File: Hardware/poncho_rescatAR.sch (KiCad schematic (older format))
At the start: 20 parts

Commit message: Arreglos en base a los hablado con el profesor
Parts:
- removed C? (x2): 100nF, ~, symbol C
- removed P?: CONN_4, symbol CONN_4
- removed R? (x2): 10k, ~, symbol R
- removed R? (x2): 1k, ~, symbol R
- removed SW? (x2): SW_PUSH, ~, symbol SW_PUSH
- removed U?: LM317AH, TO-39, symbol LM317AH
- added C1: 0.1u, ~, symbol CP1
- added D2, D3: DIODE, ~, symbol DIODE
- added JP1: JUMPER3, ~, symbol JUMPER3
- added P1: CONN_I2C, symbol CONN_5
- added R4: 10k, ~, symbol R
- gave numbers to parts that had none: 6
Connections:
- net labels added: 3.8V_II, UART2_RXD, UART2_TXD, VCC, VCC_3.8V_I, VCC_5V_EXT
- net labels removed: +3.3V, +5V, GNDA
- wire segments 166 -> 153
- no-connect marks 87 -> 95
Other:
- note added: "Bateria de celular:"
- note added: "Este conector es para\nagregar el modulo GPS\n"
- note added: "Estos son los\nAnalog_GND\nque no usamos"
- note added: "Fuente externa\npara la ciaa tambien"
- note added: "Habria que ver esto si pasa algo\nque int, xda y xcl esten en GND.\nAD0 debe estar a GND para\nseleccionar la direccion 0x68"
- note added: "Los "X" que no tienen comentarios\n son los que estan sin asignar en el\nesquematico del fabricante, o pines\nque no utilizamos\n"
- note added: "OJO: La ciaa tiene otro uart??\npor lo que vi tiene UART0 en\nlos pines:\nGPIO1=TXD\nGPIO2=RXD\nHay que probar"
- note added: "Rx de la edu-ciaa se conecta con\nRx del esquematico del GE864 Rx \ntambien (Lo determinamos por\nprueba y error)"
- note added: "estos flags "Not connect" van\na estar hasta que averiguemos\nbien con que pin debe ir conectado"
- note removed: "Este conector de 4 es para extender\nfuncionalidades facilmente en un futuro."
- note removed: "Los "X" que no tienen comentarios\n son los que estan sin asignar en el\n esquematico del fabricante.\n\nLos wires de SO101 que no tienen \nnombre son GND, preguntar:\n+>Que GND conviene poner??\n+>Que diferencia tienen??\n\n"

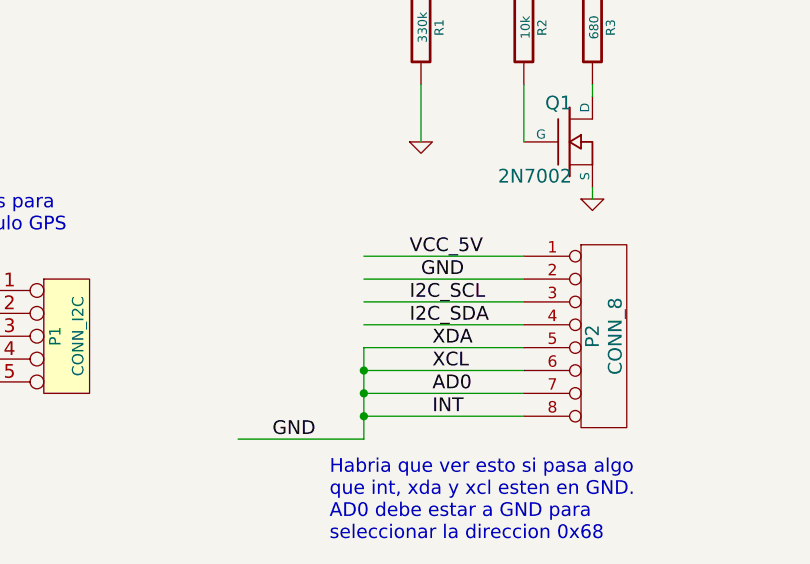
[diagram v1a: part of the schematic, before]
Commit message: cambio conector del MPU  en el esquematico
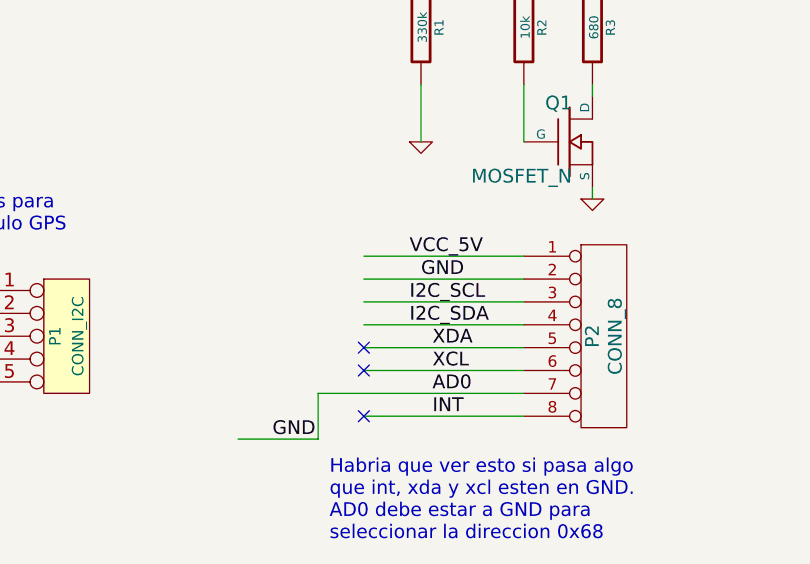
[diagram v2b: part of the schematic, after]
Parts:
- Q1: value 2N7002 -> MOSFET_N
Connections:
- no-connect marks 95 -> 98
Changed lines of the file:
@@
 Sheet 1 1
 Title "poncho_rescatAR"
-Date "29 oct 2015"
+Date "4 nov 2015"
 Rev "0.1"
 Comp ""
@@
 P 5900 6250
 F 0 "Q1" H 5910 6420 60  0000 R CNN
-F 1 "2N7002" H 5910 6100 60  0000 R CNN
+F 1 "MOSFET_N" H 5910 6100 60  0000 R CNN
 F 2 "~" H 5900 6250 60  0000 C CNN
 F 3 "~" H 5900 6250 60  0000 C CNN
@@
 	5700 7450 5000 7450
 Wire Wire Line
-	5000 7350 5700 7350
+	4800 7350 5700 7350
 Wire Wire Line
 	5700 7250 5000 7250
@@
 Wire Wire Line
 	2650 7200 3300 7200
-Wire Wire Line
-	5000 7150 5000 7550
-Wire Wire Line
-	5000 7550 4450 7550
 Wire Wire Line
 	6350 3400 5800 3400
@@
 VCC_5V
 NoConn ~ 6350 3600
-Connection ~ 5000 7250
-Connection ~ 5000 7350
-Connection ~ 5000 7450
 Connection ~ 8800 800
 NoConn ~ 2150 2900
@@
 	1    0    0    -1
 $EndComp
+NoConn ~ 5000 7450
+NoConn ~ 5000 7150
+NoConn ~ 5000 7250
+Wire Wire Line
+	4800 7350 4800 7550
+Wire Wire Line
+	4800 7550 4450 7550
 $EndSCHEMATC

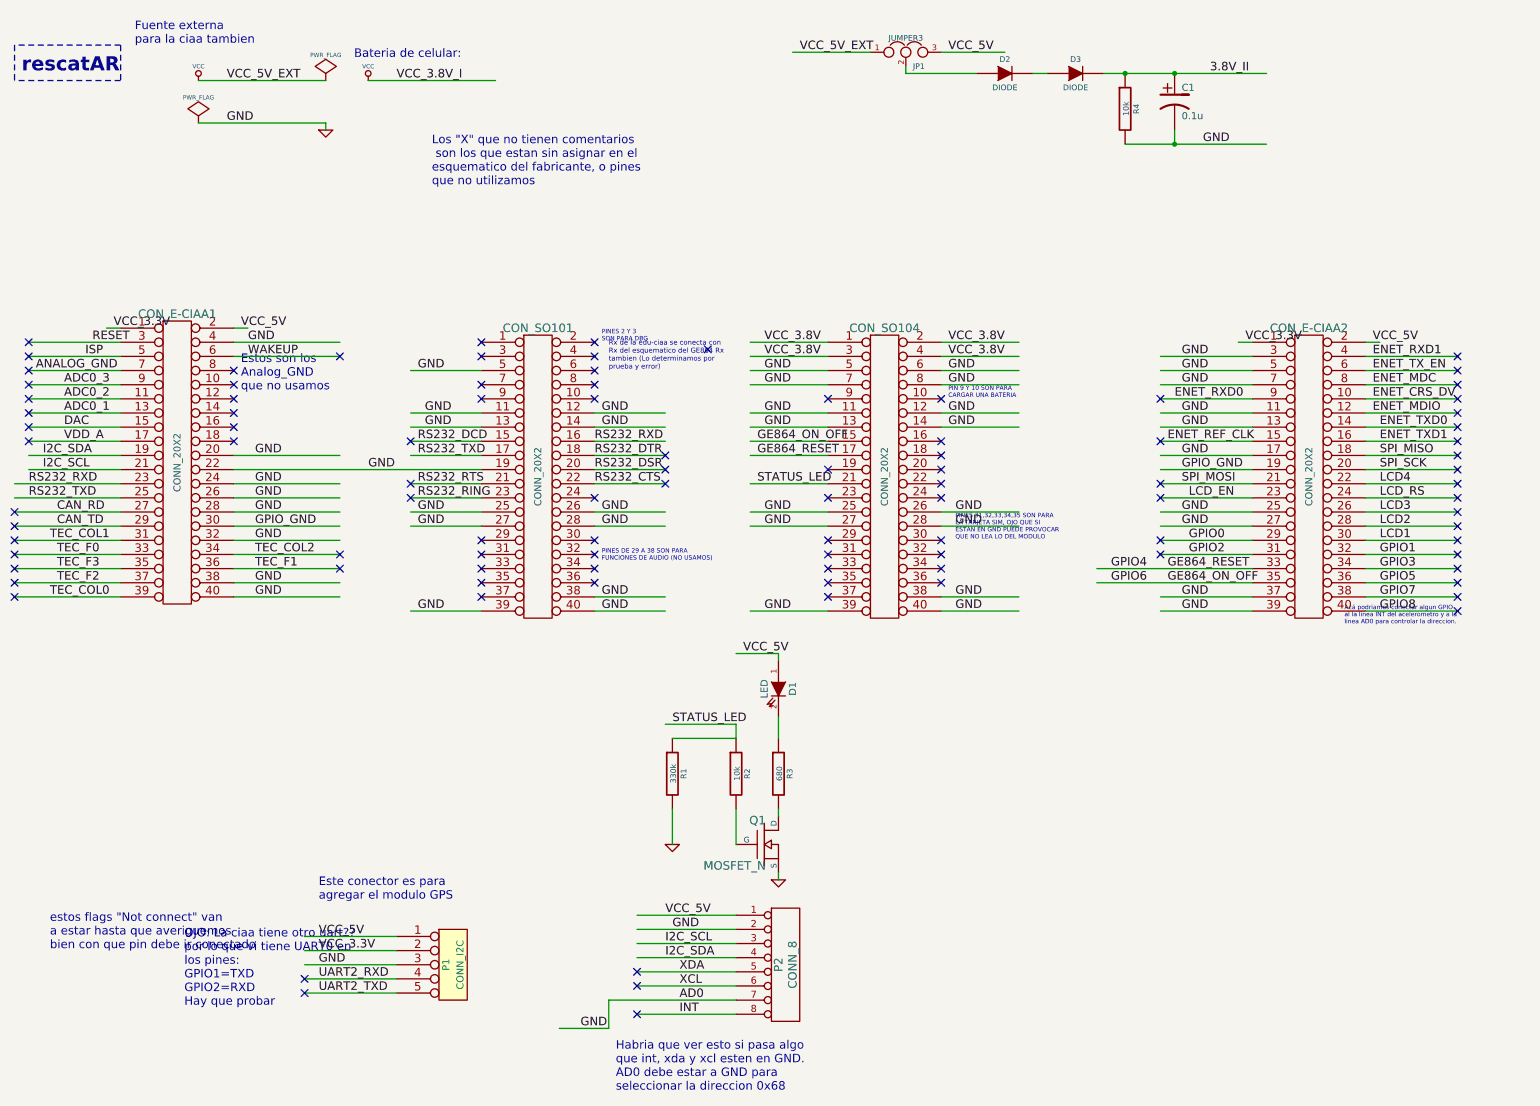
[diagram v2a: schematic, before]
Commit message: simplificacion del esquematico y comienzo del PCB
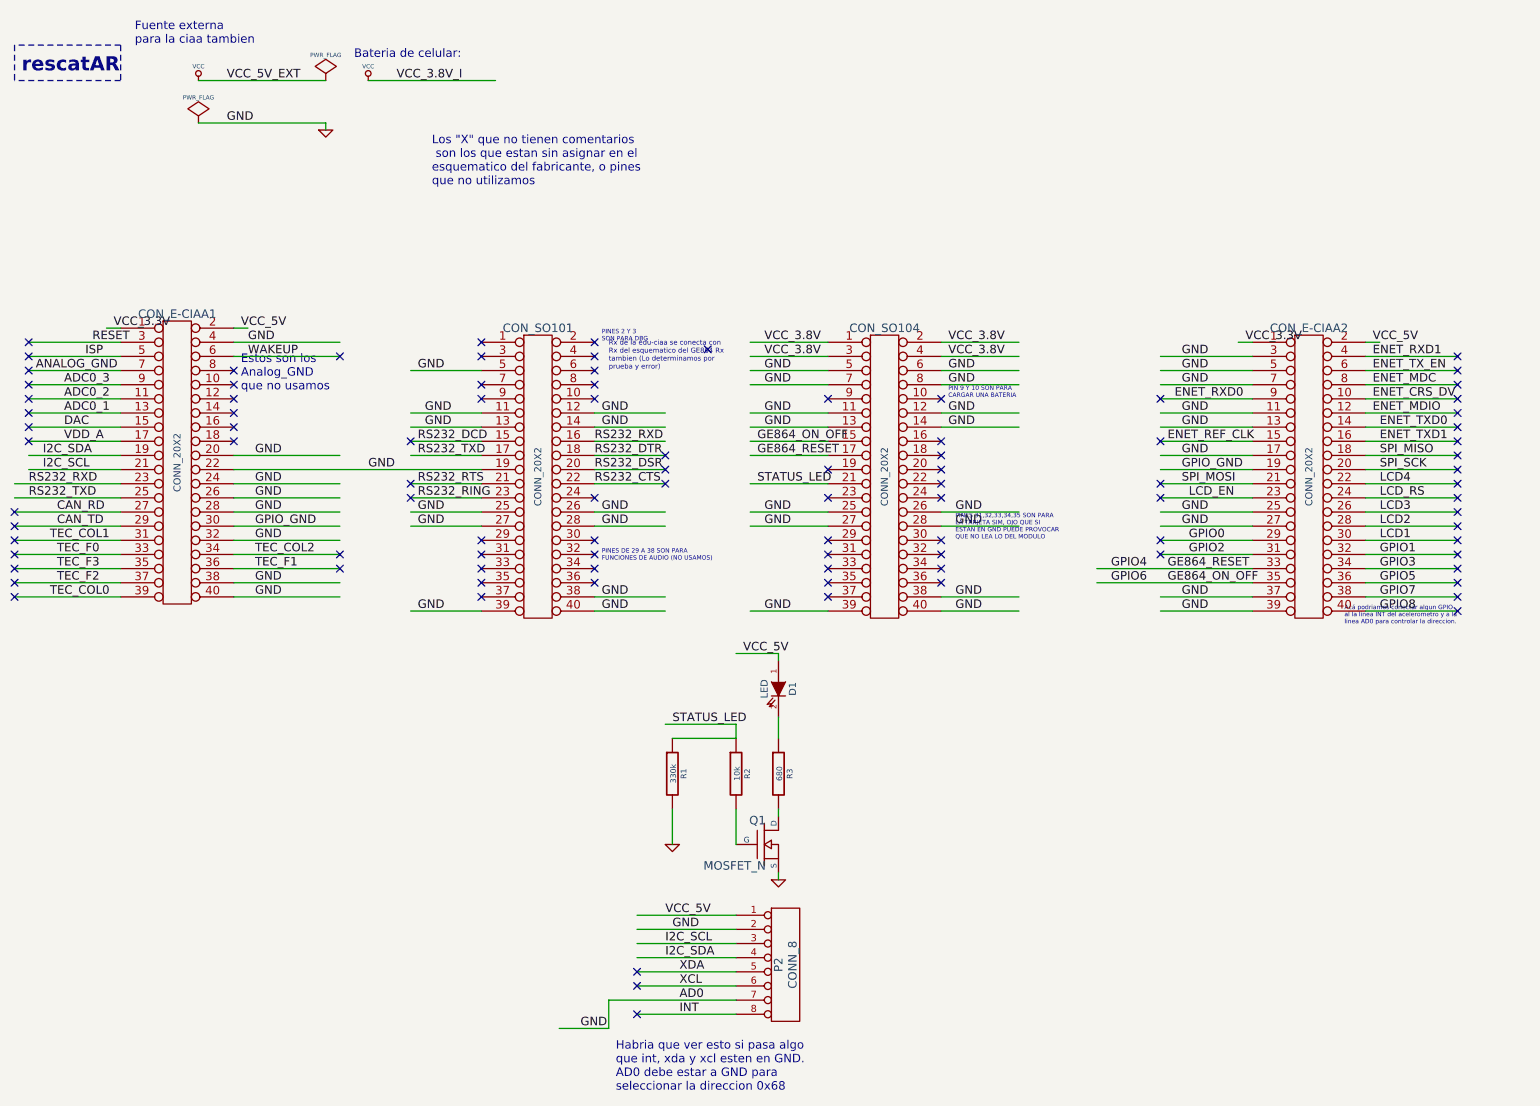
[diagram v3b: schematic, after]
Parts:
- removed C1: 0.1u, ~, symbol CP1
- removed D2, D3: DIODE, ~, symbol DIODE
- removed JP1: JUMPER3, ~, symbol JUMPER3
- removed P1: CONN_I2C, symbol CONN_5
- removed R4: 10k, ~, symbol R
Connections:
- net labels removed: 3.8V_II, UART2_RXD, UART2_TXD
- wire segments 153 -> 140
- no-connect marks 98 -> 96
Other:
- note removed: "Este conector es para\nagregar el modulo GPS\n"
- note removed: "OJO: La ciaa tiene otro uart??\npor lo que vi tiene UART0 en\nlos pines:\nGPIO1=TXD\nGPIO2=RXD\nHay que probar"
- note removed: "estos flags "Not connect" van\na estar hasta que averiguemos\nbien con que pin debe ir conectado"
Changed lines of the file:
@@
 LIBS:contrib
 LIBS:valves
+LIBS:w_connectors
 LIBS:poncho_rescatAR-cache
 EELAYER 27 0
@@
 Bateria de celular:
 NoConn ~ 5500 2750
-$Comp
-L CONN_5 P1
-U 1 1 5630390E
-P 3700 7100
-F 0 "P1" V 3650 7100 50  0000 C CNN
-F 1 "CONN_I2C" V 3750 7100 50  0000 C CNN
-F 2 "" H 3700 7100 60  0000 C CNN
-F 3 "" H 3700 7100 60  0000 C CNN
-	1    3700 7100
-	1    0    0    -1
-$EndComp
-Text Label 2750 6900 0    60   ~ 0
-VCC_5V
-Text Label 2750 7100 0    60   ~ 0
-GND
-Text Label 2750 7000 0    60   ~ 0
-VCC_3.3V
-Text Notes 2750 6650 0    60   ~ 0
-Este conector es para\nagregar el modulo GPS\n
-Text Label 2750 7300 0    60   ~ 0
-UART2_TXD
-Text Label 2750 7200 0    60   ~ 0
-UART2_RXD
-Text Notes 1800 7400 0    60   ~ 0
-OJO: La ciaa tiene otro uart??\npor lo que vi tiene UART0 en\nlos pines:\nGPIO1=TXD\nGPIO2=RXD\nHay que probar
 Text Label 5250 6850 0    60   ~ 0
 GND
@@
 	3100 850  4000 850
 Wire Wire Line
-	3300 7100 2650 7100
-Wire Wire Line
-	2650 7000 3300 7000
-Wire Wire Line
-	3300 6900 2650 6900
-Wire Wire Line
-	3300 7300 2650 7300
-Wire Wire Line
-	2650 7200 3300 7200
-Wire Wire Line
 	6350 3400 5800 3400
 Wire Wire Line
@@
 Text Label 8750 4400 0    60   ~ 0
 GE864_ON_OFF
-$Comp
-L DIODE D2
-U 1 1 56327DFE
-P 7600 800
-F 0 "D2" H 7600 900 40  0000 C CNN
-F 1 "DIODE" H 7600 700 40  0000 C CNN
-F 2 "~" H 7600 800 60  0000 C CNN
-F 3 "~" H 7600 800 60  0000 C CNN
-	1    7600 800
-	1    0    0    -1
-$EndComp
-$Comp
-L DIODE D3
-U 1 1 56327E0B
-P 8100 800
-F 0 "D3" H 8100 900 40  0000 C CNN
-F 1 "DIODE" H 8100 700 40  0000 C CNN
-F 2 "~" H 8100 800 60  0000 C CNN
-F 3 "~" H 8100 800 60  0000 C CNN
-	1    8100 800
-	1    0    0    -1
-$EndComp
-$Comp
-L R R4
-U 1 1 56327E16
-P 8450 1050
-F 0 "R4" V 8530 1050 40  0000 C CNN
-F 1 "10k" V 8457 1051 40  0000 C CNN
-F 2 "~" V 8380 1050 30  0000 C CNN
-F 3 "~" H 8450 1050 30  0000 C CNN
-	1    8450 1050
-	1    0    0    -1
-$EndComp
-Wire Wire Line
-	7800 800  7900 800
-Wire Wire Line
-	8300 800  9450 800
-$Comp
-L CP1 C1
-U 1 1 56328277
-P 8800 1000
-F 0 "C1" H 8850 1100 50  0000 L CNN
-F 1 "0.1u" H 8850 900 50  0000 L CNN
-F 2 "~" H 8800 1000 60  0000 C CNN
-F 3 "~" H 8800 1000 60  0000 C CNN
-	1    8800 1000
-	1    0    0    -1
-$EndComp
-Connection ~ 8450 800
-Wire Wire Line
-	8450 1300 9450 1300
-Text Label 9000 1300 0    60   ~ 0
-GND
-Wire Wire Line
-	8800 1200 8800 1300
-Connection ~ 8800 1300
-Text Label 9050 800  0    60   ~ 0
-3.8V_II
-Wire Wire Line
-	7400 800  6900 800
-Text Label 7200 650  0    60   ~ 0
-VCC_5V
 $Comp
 L GND #PWR04
@@
 Wire Wire Line
 	2800 1150 1900 1150
-$Comp
-L JUMPER3 JP1
-U 1 1 5632868F
-P 6900 650
-F 0 "JP1" H 6950 550 40  0000 L CNN
-F 1 "JUMPER3" H 6900 750 40  0000 C CNN
-F 2 "~" H 6900 650 60  0000 C CNN
-F 3 "~" H 6900 650 60  0000 C CNN
-	1    6900 650
-	1    0    0    -1
-$EndComp
-Wire Wire Line
-	6900 800  6900 750
-Wire Wire Line
-	7150 650  7600 650
-Wire Wire Line
-	6650 650  6100 650
-Text Label 6150 650  0    60   ~ 0
-VCC_5V_EXT
-NoConn ~ 2650 7200
-NoConn ~ 2650 7300
-Text Notes 850  7000 0    60   ~ 0
-estos flags "Not connect" van\na estar hasta que averiguemos\nbien con que pin debe ir conectado
 Wire Wire Line
 	6000 4900 5700 4900
@@
 VCC_5V
 NoConn ~ 6350 3600
-Connection ~ 8800 800
 NoConn ~ 2150 2900
 NoConn ~ 2150 3000

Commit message: cambios en el esquematico con el regulador de tension para el modulo telit, y el zocalo para la bateria
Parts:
- removed Q1: MOSFET_N, ~, symbol MOSFET_N
- added BAT?: BAT_CONN, ~, symbol BAT_CONN
- added C?: CP1, ~, symbol CP1
- added D?: ZENER, ~, symbol ZENER
- added JP? (x2): JUMPER3, ~, symbol JUMPER3
- added P?: CONN_2, symbol CONN_2
- added Q1: BC547, TO92, symbol BC547
- added Q?: BC338, TO92, symbol BC338
- added R?: R, ~, symbol R
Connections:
- net labels added: VCC_3.8V_II
- net labels removed: GPIO_GND
- wire segments 140 -> 161

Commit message: retoques finales al esquemetico y pcb base
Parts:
- removed C?: CP1, ~, symbol CP1
- removed D?: ZENER, ~, symbol ZENER
- removed JP? (x2): JUMPER3, ~, symbol JUMPER3
- removed P?: CONN_2, symbol CONN_2
- removed Q1: BC547, TO92, symbol BC547
- removed Q?: BC338, TO92, symbol BC338
- removed R2: 10k, ~, symbol R
- removed R3: 680, ~, symbol R
- removed R?: R, ~, symbol R
- added C1, C2: 10uF, ~, symbol CP1
- added C3, C4, C5, C6: 0.1, ~, symbol C
- added P1: 5V_OUT, symbol CONN_2
- added R4: 470, ~, symbol R
- added R5: 220, ~, symbol R
- added U1: LM317T, TO-220, symbol LM317T
- added U2: LM7805, symbol LM7805
- R1: value 330k -> 330
- gave numbers to parts that had none: 1
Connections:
- net labels added: VCC_12V
- net labels removed: AD0, VCC_3.8V_I, VCC_3.8V_II, VCC_5V_EXT
- wire segments 161 -> 156
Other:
- note removed: "Bateria de celular:"
- note removed: "Fuente externa\npara la ciaa tambien"
- note removed: "Habria que ver esto si pasa algo\nque int, xda y xcl esten en GND.\nAD0 debe estar a GND para\nseleccionar la direccion 0x68"
